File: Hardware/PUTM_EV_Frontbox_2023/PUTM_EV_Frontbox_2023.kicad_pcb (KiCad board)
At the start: 4 copper layers, 97 x 70 mm, 232 parts, among them J1 Conn_02x15_Counter_Clockwise, J3 STLINK-V3MINIE, K2 FINDER-32.21-x000, Q1 NX7002AK, U1 STM32G473RCTx, U10 TLP291-4, U11 TLP291-4, U12 MCP2542FDxMF, U13 MCP6001, U14 MCP6N11-005, U15 MCP6001, U16 MCP6N11-005, U17 MCP6002-xMC, U18 MCP6N11-005, U19 TLV743P, U2 MCP6002-xMC, U20 LM4040DBZ-5, U21 MCP6001, U22 MCP6N11-005, U23 MCP6001, U24 MCP6001, U25 MCP6N11-005, U26 MCP6001, U3 IMS330DHCX, U4 TLV743P, U5 TLV743P, U6 BD50FC0FP, U7 LM62440-Q1, U8 MCP2542FDxMF, U9 MCP6N11-005, Y1 ABM8G-48.000MHZ

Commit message: Board review
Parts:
- H1, H2, H3, H4: footprint MountingHole:MountingHole_3.2mm_M3_DIN965_Pad_TopBottom -> MountingHole:MountingHole_3.2mm_M3_Pad_Via
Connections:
- U1 pad 56: /IMU_CLK -> /Safety_control
- U1 pad 57: /IMU_MISO -> unconnected-(U1-PB4-Pad57)
- U1 pad 58: /IMU_MOSI -> unconnected-(U1-PB5-Pad58)
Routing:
- net /APPS2_3V3: track 109.4 -> 49.2 mm, vias 12 -> 2
- net /Safety_control: track 0.00 -> 36.2 mm, vias 0 -> 2
- net Net-(U23-+): track 39.1 -> 6.51 mm
- net GND: track 248.9 -> 216.6 mm, vias 173 -> 153
- net Net-(U22-FG): track 38.1 -> 6.35 mm, vias 12 -> 2
- net /APPS_POT_2: track 55.7 -> 24.9 mm
- net /APPS_sig2: track 74.0 -> 43.9 mm
- net Net-(R56-Pad2): track 38.7 -> 14.4 mm
- net Net-(C58-Pad1): track 21.2 -> 3.53 mm
- net Net-(U22-EN): track 14.9 -> 2.48 mm
- net /DAC2_REF: track 45.0 -> 33.8 mm
- net +24V: track 2.82 -> 12.9 mm
- net Net-(U17B--): track 26.7 -> 18.0 mm
- net Net-(R61-Pad2): track 9.11 -> 4.55 mm
- net /LEFT_WHEEL_SC: track 17.4 -> 20.1 mm
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- removed copper zone on F.Cu, net +24V
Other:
- board text added: "import templatki"
- board text added: "rosunąć cany"
- board text added: "wylać mase na wszystkich waestwach"
- board text added: "zmienic tp na uszka"

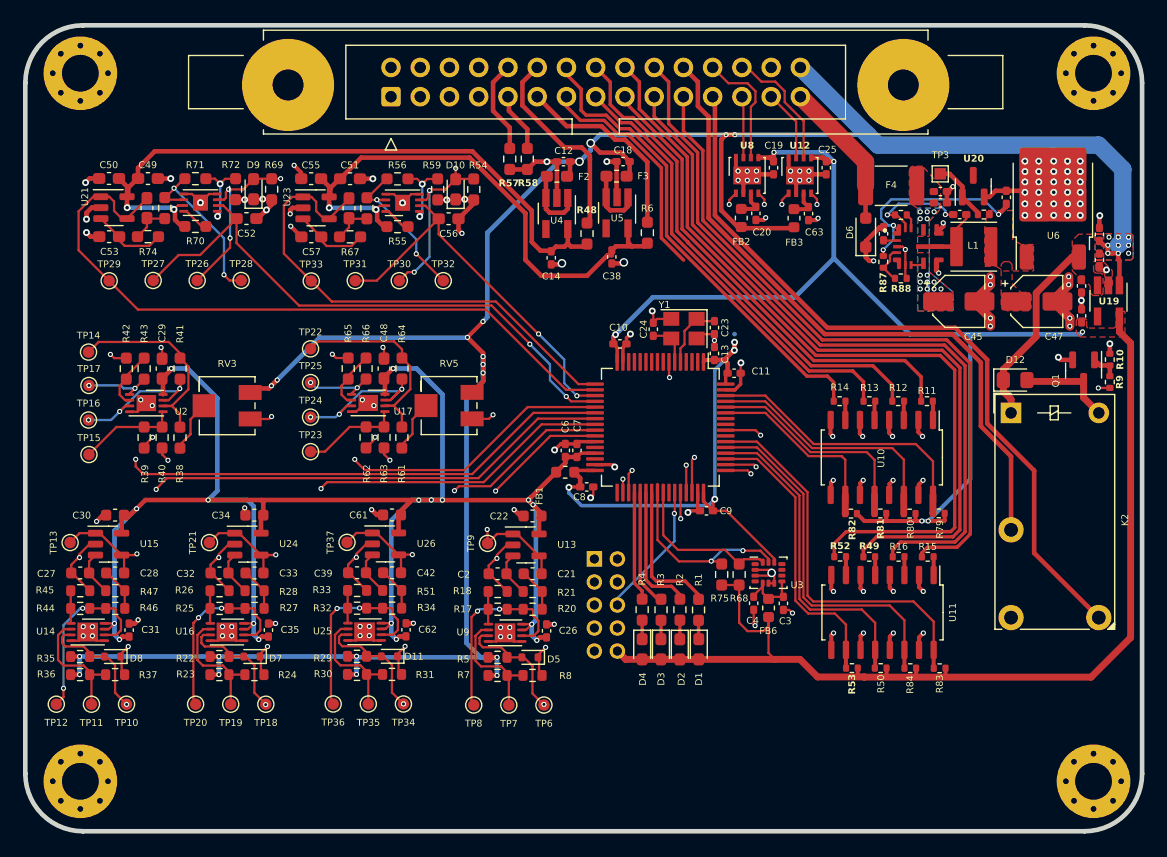
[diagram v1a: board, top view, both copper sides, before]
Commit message: Moved sw cap closer to pins
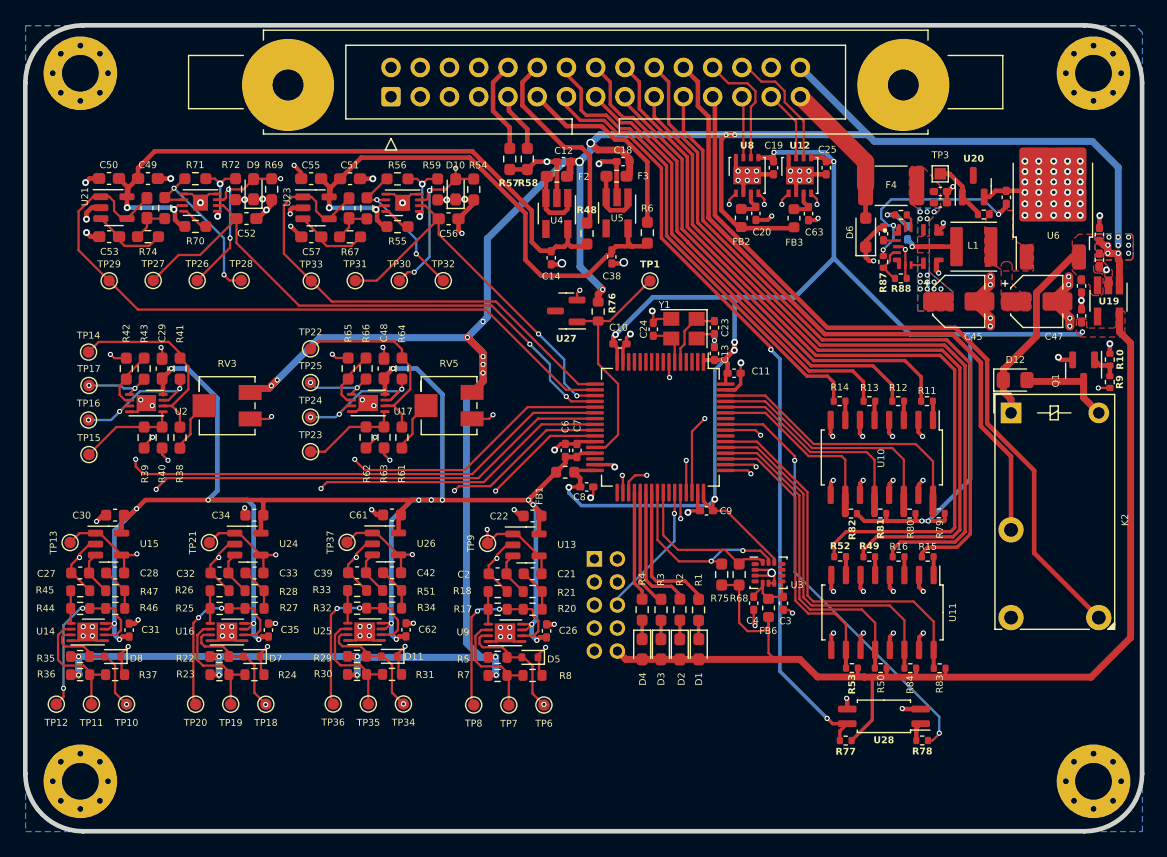
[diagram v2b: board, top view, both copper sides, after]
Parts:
- added R76: 1k, Resistor_SMD:R_0603_1608Metric, F.Cu at (154.7, 42.8)
- added R77: 10k, Resistor_SMD:R_0402_1005Metric, F.Cu at (176.2, 80.1)
- added R78: 2k, Resistor_SMD:R_0402_1005Metric, F.Cu at (182.9, 80.1)
- added TP1: TestPoint_Small, TestPoint:TestPoint_Pad_D1.0mm, F.Cu at (159.2, 40.2)
- added U27: LM4040C33FTA, Package_TO_SOT_SMD:SOT-23, F.Cu at (152.0, 42.8)
- added U28: FODM217B, Package_SO:SOP-4_4.4x2.6mm_P1.27mm, F.Cu at (179.6, 78.0)
- C46: moved to B.Cu
- moved C46 4.81 mm to (181.6, 36.0), turned to 90 degrees
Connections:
- U1 pad 28: unconnected-(U1-VREF+-Pad28) -> /VREF
- U1 pad 57: unconnected-(U1-PB4-Pad57) -> /Sense_Left_Wheel
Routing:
- net /LEFT_WHEEL_SC: track 20.1 -> 68.9 mm, vias 0 -> 2
- net /Sense_Left_Wheel: track 0.00 -> 37.7 mm, vias 0 -> 2
- net /VREF: track 0.00 -> 20.9 mm
- net +5V: track 235.4 -> 248.8 mm, vias 28 -> 29
- net +3.3V: track 236.1 -> 246.4 mm
- net GND: track 216.6 -> 221.4 mm, vias 153 -> 156
- net Net-(U7-CBOOT): track 9.01 -> 4.47 mm, vias 2 -> 1
- net Net-(R78-Pad2): track 0.00 -> 1.62 mm
- net /CAN2_RX: track 37.0 -> 38.4 mm
- net /CAN2_TX: track 35.2 -> 34.4 mm
- net Net-(U7-SW): track 5.46 -> 6.23 mm, vias 0 -> 1
- net /IMU_SCL: track 17.3 -> 16.6 mm
- added copper zone on B.Cu, net GND
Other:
- board text removed: "import templatki"
- board text removed: "rosunąć cany"
- board text removed: "wylać mase na wszystkich waestwach"
- board text removed: "zmienic tp na uszka"

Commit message: Production files
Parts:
- removed C15, C16: 1uF, Capacitor_SMD:C_0402_1005Metric_Pad0.74x0.62mm_HandSolder
- removed C17: 10nF, Capacitor_SMD:C_0402_1005Metric_Pad0.74x0.62mm_HandSolder
- removed D6: SD24_SOD323, Diode_SMD:D_SOD-323_HandSoldering
- removed F4: 1.5A, Fuse:Fuse_1812_4532Metric_Pad1.30x3.40mm_HandSolder
- removed R19: 200R, Resistor_SMD:R_0402_1005Metric
- removed R88: 16k7, Resistor_SMD:R_0402_1005Metric
- removed R89: 0R, Resistor_SMD:R_0402_1005Metric
- removed TP3: TestPoint, TestPoint:TestPoint_Pad_1.0x1.0mm
- removed U20: LM4040DBZ-5, Package_TO_SOT_SMD:SOT-23
- removed U6: BD50FC0FP, Package_TO_SOT_SMD:TO-252-2
- added C1: 2u2, Capacitor_SMD:C_0805_2012Metric, F.Cu at (180.8, 37.1)
- added C40: 4u7, Capacitor_SMD:C_0805_2012Metric, F.Cu at (182.9, 37.1)
- added C5: 2u2, Capacitor_SMD:C_0805_2012Metric, F.Cu at (178.8, 37.1)
- added C59: 22u, Capacitor_SMD:C_0603_1608Metric, F.Cu at (185.2, 40.4)
- added C60: 22u, Capacitor_SMD:C_0603_1608Metric, F.Cu at (191.3, 40.4)
- added F1: 1.5A, Fuse:Fuse_1812_4532Metric, F.Cu at (178.6, 32.4)
- added L2: 1u5, Inductor_SMD:L_Abracon_ASPI-4030S, F.Cu at (188.2, 39.6)
- added R85: 100k, Resistor_SMD:R_0603_1608Metric, F.Cu at (187.7, 30.2)
- added R86: 24k9, Resistor_SMD:R_0603_1608Metric, F.Cu at (186.2, 30.2)
- added TP2: TestPoint_Small, TestPoint:TestPoint_Pad_D1.0mm, F.Cu at (195.1, 32.2)
- C41: value 220nF -> 4u7; footprint Capacitor_SMD:C_0402_1005Metric_Pad0.74x0.62mm_HandSolder -> Capacitor_SMD:C_0805_2012Metric
- C43: value 1uF -> 220n; footprint Capacitor_SMD:C_0402_1005Metric_Pad0.74x0.62mm_HandSolder -> Capacitor_SMD:C_0805_2012Metric
- C44: value 220nF -> 1u; footprint Capacitor_SMD:C_0402_1005Metric_Pad0.74x0.62mm_HandSolder -> Capacitor_SMD:C_0603_1608Metric
- C45: value 4u7F -> 220n; footprint Capacitor_SMD:CP_Elec_4x5.7 -> Capacitor_SMD:C_0805_2012Metric
- C46: value 100nF -> 100n; footprint Capacitor_SMD:C_0402_1005Metric_Pad0.74x0.62mm_HandSolder -> Capacitor_SMD:C_0603_1608Metric; moved to F.Cu
- C47: value 10uF -> 22p; footprint Capacitor_SMD:CP_Elec_4x5.7 -> Capacitor_SMD:C_0603_1608Metric
- L1: value 2u2H -> 1u5
- R87: value 100k -> 1k; footprint Resistor_SMD:R_0402_1005Metric -> Resistor_SMD:R_0603_1608Metric
- U7: footprint Frontbox:IC_LM61460AANRJRR -> footprints:IC_LM61460AANRJRR
- moved R87 15.6 mm to (192.7, 30.2), turned to 90 degrees
- moved C43 14.1 mm to (193.6, 37.1), turned to -90 degrees
- moved C47 12.3 mm to (189.2, 30.2), turned to -90 degrees
- moved C46 9.88 mm to (191.2, 33.8)
- moved C45 7.32 mm to (191.5, 37.1), turned to -90 degrees
- moved C44 7.22 mm to (190.9, 30.2), turned to 90 degrees
- moved U7 6.17 mm to (188.2, 34.8), turned to -90 degrees
- moved L1 6.04 mm to (183.0, 33.0)
- moved C41 4.73 mm to (184.9, 37.1), turned to -90 degrees
- moved U19 4.20 mm to (198.4, 37.8)
- moved C36 4.20 mm to (196.1, 39.0)
- moved C37 4.20 mm to (196.1, 36.5)
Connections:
- C41 pad 1: Net-(U7-EN) -> /Power section/VIN
- C43 pad 1: Net-(U7-VCC) -> /Power section/VIN
- C44 pad 1: Net-(U7-EN) -> Net-(U7-VCC)
- C45 pad 1: Net-(U7-EN) -> /Power section/VIN
- C46 pad 1: Net-(U7-SW) -> /Power section/SW
- C47 pad 1: +7.5V -> Net-(C47-Pad1)
- C47 pad 2: GND -> /Power section/FB
- L1 pad 1: Net-(U7-SW) -> /Power section/+24V_FUSED
- L1 pad 2: +7.5V -> /Power section/VIN
- R87 pad 1: +7.5V -> +5V
- R87 pad 2: Net-(U7-FB) -> Net-(C47-Pad1)
- U7 pad 1: +7.5V -> +5V
- U7 pad 10: Net-(U7-SW) -> /Power section/SW
- U7 pad 12: Net-(U7-EN) -> /Power section/VIN
- U7 pad 13: Net-(U7-RBOOT) -> Net-(U7-CBOOT)
- U7 pad 4: Net-(U7-FB) -> /Power section/FB
- U7 pad 7: Net-(U7-EN) -> /Power section/VIN
- U7 pad 8: Net-(U7-EN) -> /Power section/VIN
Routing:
- net +7.5V: track 18.3 -> 0.00 mm, vias 3 -> 0
- net GND: track 221.4 -> 206.6 mm, vias 156 -> 139
- net +3.3V: track 246.4 -> 254.8 mm, vias 10 -> 14
- net /Power section/SW: track 0.00 -> 6.52 mm
- net Net-(U7-SW): track 6.23 -> 0.00 mm, vias 1 -> 0
- net 5v_ref: track 5.37 -> 0.00 mm
- net /Power section/FB: track 0.00 -> 5.20 mm
- net +24V: track 12.9 -> 8.00 mm
- net Net-(C47-Pad1): track 0.00 -> 4.23 mm
- net Net-(U7-FB): track 3.41 -> 0.00 mm
- net Net-(U7-VCC): track 1.18 -> 3.79 mm
- net Net-(U7-CBOOT): track 4.47 -> 2.17 mm, vias 1 -> 0
- net +5V: track 248.8 -> 250.6 mm, vias 29 -> 19
- net /Power section/VIN: track 0.00 -> 1.58 mm, vias 0 -> 9
- net Net-(U7-RBOOT): track 1.31 -> 0.00 mm
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- added copper zone on F.Cu, net /Power section/+24V_FUSED
- added copper zone on B.Cu, net /Power section/VIN
- added copper zone on F.Cu, net /Power section/VIN
- removed copper zone on B.Cu, net +5V
- removed copper zone on F.Cu, net +7.5V
- removed copper zone on B.Cu, net Net-(U7-EN)
- removed copper zone on F.Cu, net Net-(U7-EN)
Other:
- board text added: "Adam Wasilewski"

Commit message: New firmware
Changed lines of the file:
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@@
     (fp_line (start 2.25 1.6) (end -2.25 1.6)
       (stroke (width 0.1) (type solid)) (layer "F.Fab"))
-    (pad "1" smd roundrect (at -2.1375 0 270) (size 1.125 3.4) (layers "F.Cu" "F.Paste" "F.Mask") (roundrect_rratio 0.222222)
+    (pad "1" smd roundrect (at -2.1375 0 270) (size 1.125 3.4) (layers "F.Cu" "F.Paste" "F.Mask") (roundrect_rratio 0.2222222222)
       (net 18 "+24V") (pintype "passive"))
-    (pad "2" smd roundrect (at 2.1375 0 270) (size 1.125 3.4) (layers "F.Cu" "F.Paste" "F.Mask") (roundrect_rratio 0.222222)
+    (pad "2" smd roundrect (at 2.1375 0 270) (size 1.125 3.4) (layers "F.Cu" "F.Paste" "F.Mask") (roundrect_rratio 0.2222222222)
       (net 8 "/Power section/+24V_FUSED") (pintype "passive"))
     (model "${KICAD6_3DMODEL_DIR}/Fuse.3dshapes/Fuse_1812_4532Metric.wrl"
